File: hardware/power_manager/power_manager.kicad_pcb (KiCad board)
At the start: 2 copper layers, 31 x 25.5 mm, 14 parts, among them J1 Conn_01x02_Pin, J2 Conn_01x02_Pin, J3 Conn_01x02_Pin, U1 TP4054-SOT25R, U2 AP2112K-3.3

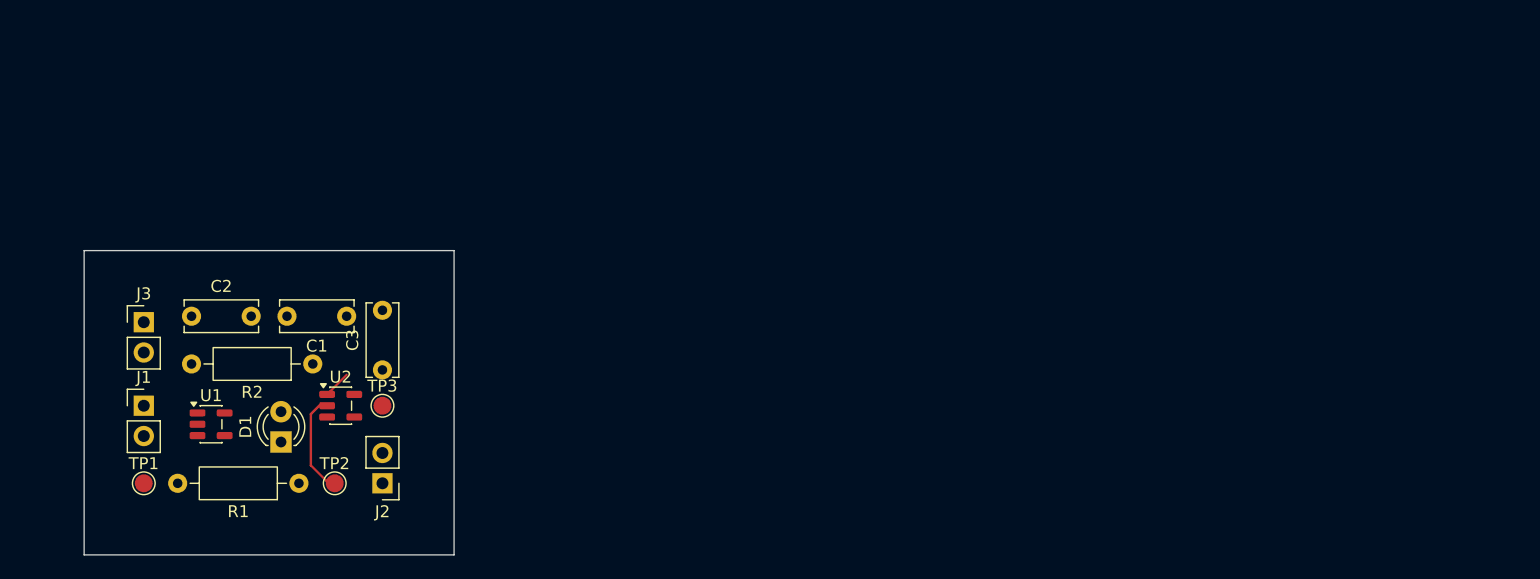
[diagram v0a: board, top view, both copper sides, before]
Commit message: Imp: powermanager schematic v0.2
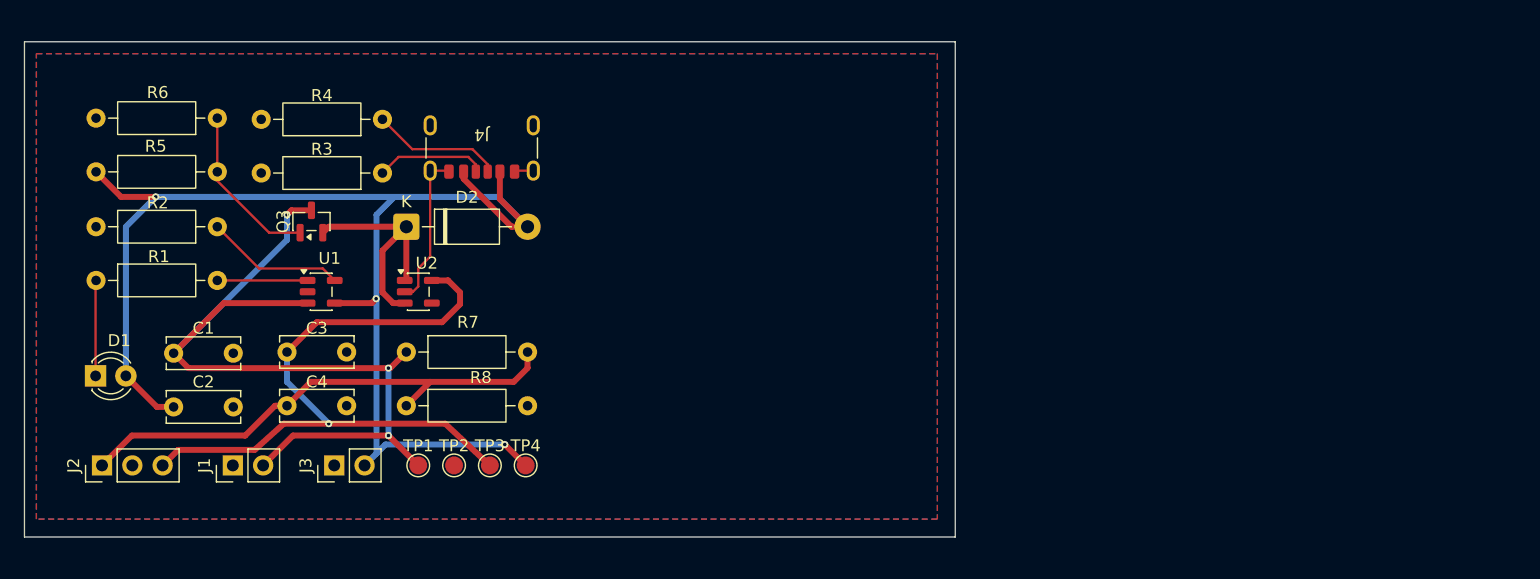
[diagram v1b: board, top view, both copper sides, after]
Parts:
- added C4: 100nF, Capacitor_THT:C_Disc_D6.0mm_W2.5mm_P5.00mm, F.Cu at (43.5, 65.5)
- added D2: 1N5819, Diode_THT:D_DO-41_SOD81_P10.16mm_Horizontal, F.Cu at (53.5, 50.5)
- added J4: USB_C_Receptacle_PowerOnly_6P, Connector_USB:USB_C_Receptacle_GCT_USB4125-xx-x_6P_TopMnt_Horizontal, F.Cu at (59.8, 42.8)
- added Q3: AO3401A, Package_TO_SOT_SMD:SOT-23, F.Cu at (45.5, 50.1)
- added R3: 5.1k, Resistor_THT:R_Axial_DIN0207_L6.3mm_D2.5mm_P10.16mm_Horizontal, F.Cu at (51.5, 46.0)
- added R4: 5.1k, Resistor_THT:R_Axial_DIN0207_L6.3mm_D2.5mm_P10.16mm_Horizontal, F.Cu at (51.5, 41.5)
- added R5: 1k, Resistor_THT:R_Axial_DIN0207_L6.3mm_D2.5mm_P10.16mm_Horizontal, F.Cu at (27.5, 45.9)
- added R6: 5.1k, Resistor_THT:R_Axial_DIN0207_L6.3mm_D2.5mm_P10.16mm_Horizontal, F.Cu at (37.7, 41.4)
- added R7: 100k, Resistor_THT:R_Axial_DIN0207_L6.3mm_D2.5mm_P10.16mm_Horizontal, F.Cu at (53.5, 61.0)
- added R8: 100k, Resistor_THT:R_Axial_DIN0207_L6.3mm_D2.5mm_P10.16mm_Horizontal, F.Cu at (53.5, 65.5)
- added TP4: TestPoint, TestPoint:TestPoint_Pad_D1.5mm, F.Cu at (63.5, 70.5)
- J2: value Conn_01x02_Pin -> Conn_01x03_Pin; footprint Connector_PinHeader_2.54mm:PinHeader_1x02_P2.54mm_Vertical -> Connector_PinHeader_2.54mm:PinHeader_1x03_P2.54mm_Vertical
- moved R1 24.0 mm to (27.5, 55.0), turned to 0 degrees
- moved J2 23.5 mm to (28.0, 70.5), turned to 90 degrees
- moved TP1 23.0 mm to (54.5, 70.5)
- moved J3 20.0 mm to (47.5, 70.5), turned to 90 degrees
- moved D1 16.5 mm to (27.5, 63.0), turned to 0 degrees
- moved C1 14.8 mm to (34.0, 61.1), turned to 0 degrees
- moved U1 14.4 mm to (46.4, 56.0)
- moved R2 14.0 mm to (37.7, 50.5)
- moved U2 11.6 mm to (54.5, 56.0)
- moved TP3 10.3 mm to (60.5, 70.5)
- moved TP2 10.1 mm to (57.5, 70.5)
- moved J1 8.98 mm to (39.0, 70.5), turned to 90 degrees
- moved C3 8.14 mm to (43.5, 61.0), turned to 0 degrees
- moved C2 7.75 mm to (34.0, 65.6)
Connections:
- net Net-(D1-A) renamed /VIN
- C1 pad 1: Net-(J1-Pin_2) -> /VBAT
- C3 pad 1: Net-(J2-Pin_2) -> /3V3
- J1 pad 2: Net-(J1-Pin_2) -> /VBAT
- J2 pad 1: GND -> /BAT_ADC
- J2 pad 2: Net-(J2-Pin_2) -> GND
- TP1 pad 1: Net-(J1-Pin_2) -> /VBAT
- TP3 pad 1: Net-(J2-Pin_2) -> /3V3
- U1 pad 3: Net-(J1-Pin_2) -> /VBAT
- U2 pad 1: Net-(J1-Pin_2) -> /VCC
- U2 pad 3: Net-(J1-Pin_2) -> /VCC
- U2 pad 5: Net-(J2-Pin_2) -> /3V3
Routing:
- net /VIN: track 0.00 -> 113.5 mm, vias 0 -> 3
- net /VBAT: track 0.00 -> 72.0 mm, vias 0 -> 3
- net /3V3: track 0.00 -> 57.6 mm, vias 0 -> 1
- net /BAT_ADC: track 0.00 -> 43.2 mm
- net /VCC: track 0.00 -> 20.3 mm
- net Net-(Q3-G): track 0.00 -> 14.1 mm
- net Net-(U1-PROG): track 0.00 -> 11.7 mm
- net Net-(J4-CC1): track 0.00 -> 11.0 mm
- net Net-(J4-CC2): track 0.00 -> 9.24 mm
- net Net-(D1-K): track 0.00 -> 8.02 mm
- net Net-(U1-~{CHRG}): track 0.23 -> 7.57 mm
- net GND: track 8.57 -> 14.6 mm
- net Net-(J1-Pin_2): track 2.39 -> 0.00 mm
- added copper zone on B.Cu, net GND
- added copper zone on F.Cu, net GND
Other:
- board size 31 x 25.5 mm -> 78 x 41.5 mm

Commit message: Add: PCB
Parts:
- removed J1, J3: Conn_01x02_Pin, Connector_PinHeader_2.54mm:PinHeader_1x02_P2.54mm_Vertical
- removed J2: Conn_01x03_Pin, Connector_PinHeader_2.54mm:PinHeader_1x03_P2.54mm_Vertical
- added C5: 100nF, Capacitor_SMD:C_0805_2012Metric, F.Cu at (96.0, 58.4)
- added C6: 10uF, Capacitor_SMD:C_0805_2012Metric, F.Cu at (89.0, 47.0)
- added C7: 100nF, Capacitor_SMD:C_0805_2012Metric, F.Cu at (92.5, 47.0)
- added C8: 100nF, Capacitor_SMD:C_0805_2012Metric, F.Cu at (80.5, 64.5)
- added D3: SMAJ5.0A, Diode_SMD:D_SMA, F.Cu at (79.5, 39.0)
- added D4: 1N5819, Diode_THT:D_DO-41_SOD81_P10.16mm_Horizontal, F.Cu at (89.0, 69.0)
- added J5: Conn_01x08_Pin, Connector_PinHeader_2.54mm:PinHeader_1x08_P2.54mm_Vertical, F.Cu at (102.0, 46.2)
- added R10: 200k, Resistor_THT:R_Axial_DIN0207_L6.3mm_D2.5mm_P10.16mm_Horizontal, F.Cu at (61.3, 69.0)
- added R11: 1k, Resistor_THT:R_Axial_DIN0207_L6.3mm_D2.5mm_P10.16mm_Horizontal, F.Cu at (61.3, 64.5)
- added R12: 300k, Resistor_THT:R_Axial_DIN0207_L6.3mm_D2.5mm_P10.16mm_Horizontal, F.Cu at (71.5, 60.0)
- added R9: 1k, Resistor_THT:R_Axial_DIN0207_L6.3mm_D2.5mm_P10.16mm_Horizontal, F.Cu at (61.3, 55.5)
- C1, C2, C4: footprint Capacitor_THT:C_Disc_D6.0mm_W2.5mm_P5.00mm -> Capacitor_SMD:C_0805_2012Metric
- C3: value 10uF -> 1uF; footprint Capacitor_THT:C_Disc_D6.0mm_W2.5mm_P5.00mm -> Capacitor_SMD:C_0805_2012Metric
- R7, R8: value 100k -> 470k
- moved D1 66.5 mm to (94.0, 64.0)
- moved C2 58.9 mm to (92.5, 58.4), turned to -90 degrees
- moved C1 55.1 mm to (89.0, 58.4), turned to -90 degrees
- moved C3 54.3 mm to (96.0, 47.0), turned to 90 degrees
- moved TP2 54.2 mm to (100.5, 37.5)
- moved TP1 53.8 mm to (97.0, 37.5)
- moved R5 49.9 mm to (75.3, 60.0)
- moved R6 49.9 mm to (85.5, 55.5)
- moved R1 48.6 mm to (75.3, 46.5)
- moved TP4 47.3 mm to (100.5, 41.0)
- moved TP3 47.0 mm to (97.0, 41.0)
- moved Q3 46.3 mm to (89.6, 64.5), turned to 0 degrees
- moved U1 43.6 mm to (89.9, 52.9)
- moved U2 41.7 mm to (96.1, 52.9)
- moved R2 37.7 mm to (75.3, 51.0), turned to 0 degrees
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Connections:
- net /BAT_ADC renamed Net-(C4-Pad1)
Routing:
- net /PLUGIN: track 0.00 -> 59.1 mm, vias 0 -> 1
- net /BAT_ADC: track 0.00 -> 51.7 mm
- net /3V3: track 57.6 -> 22.3 mm, vias 1 -> 0
- net /VBAT: track 72.0 -> 102.0 mm, vias 3 -> 4
- net /VIN: track 113.5 -> 142.1 mm, vias 3 -> 1
- net Net-(D1-K): track 8.02 -> 35.6 mm
- net Net-(C4-Pad1): track 43.2 -> 19.5 mm
- net Net-(C8-Pad1): track 0.00 -> 18.3 mm
- net GND: track 14.6 -> 0.00 mm
- net Net-(U1-PROG): track 11.7 -> 18.7 mm
- net Net-(U1-~{CHRG}): track 7.57 -> 13.8 mm
- net Net-(J4-CC1): track 11.0 -> 16.8 mm
- net Net-(J4-CC2): track 9.24 -> 14.0 mm
- net Net-(Q3-G): track 14.1 -> 11.6 mm
- net /VCC: track 20.3 -> 21.8 mm
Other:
- board size 78 x 41.5 mm -> 93.5 x 37 mm
